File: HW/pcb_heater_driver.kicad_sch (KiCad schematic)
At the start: 9 parts

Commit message: Progress
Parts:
- removed PS?: (no value), symbol Converter_ACDC:IRM-60-12
- removed U?: (no value), Package_TO_SOT_SMD:SOT-23-5, symbol Regulator_Linear:AP2112K-3.3
- added H1, H2, H5, H7, H8: (no value), symbol Mechanical:MountingHole_Pad
- added H3: (no value), symbol Mechanical:MountingHole
- added H4: MH2, MountingHole:MountingHole_3.2mm_M3_Pad_TopBottom, symbol Mechanical:MountingHole_Pad
- added SW1: MAIN_SWITCH, symbol Switch:SW_SPST
- added U1: (no value), symbol Espressif:ESP32-S2-MINI-1
- C1: renamed from C?; value (none) -> C
- Q1: renamed from Q?; value BUK9M156-100EX -> (none)
- R1: renamed from R?; value (none) -> R
- R3: renamed from R?; value (none) -> 10k
- R4: renamed from R?; value (none) -> Heater - 1.5 Ohm
- gave numbers to parts that had none: 2
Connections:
- net +12V: now also SW1.1 (A)
- net GND: now also U1.1 (GND)
- net LIVE: now also H1.1
- net NEUTRAL: now also H2.1
- new net: U1.2 (GND), U1.30 (GND), U1.42 (GND), U1.43 (GND), U1.46 (GND), U1.47 (GND), U1.48 (GND), U1.49 (GND), U1.50 (GND), U1.51 (GND), U1.52 (GND), U1.53 (GND), U1.54 (GND), U1.55 (GND), U1.56 (GND), U1.57 (GND), U1.58 (GND), U1.59 (GND), U1.60 (GND), U1.61 (GND), U1.62 (GND), U1.63 (GND), U1.64 (GND), U1.65 (GND)
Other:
- note added: "AC/DC brick"
- note added: "Current monitor"
- note added: "Heater"
- note added: "I2C address is 0x.."
- note added: "Note: 5 A max current (60 W)"
- note added: "Note: RC filter description"
- moved on the sheet: C1, Q1, R1, R2, R3, R4, U2

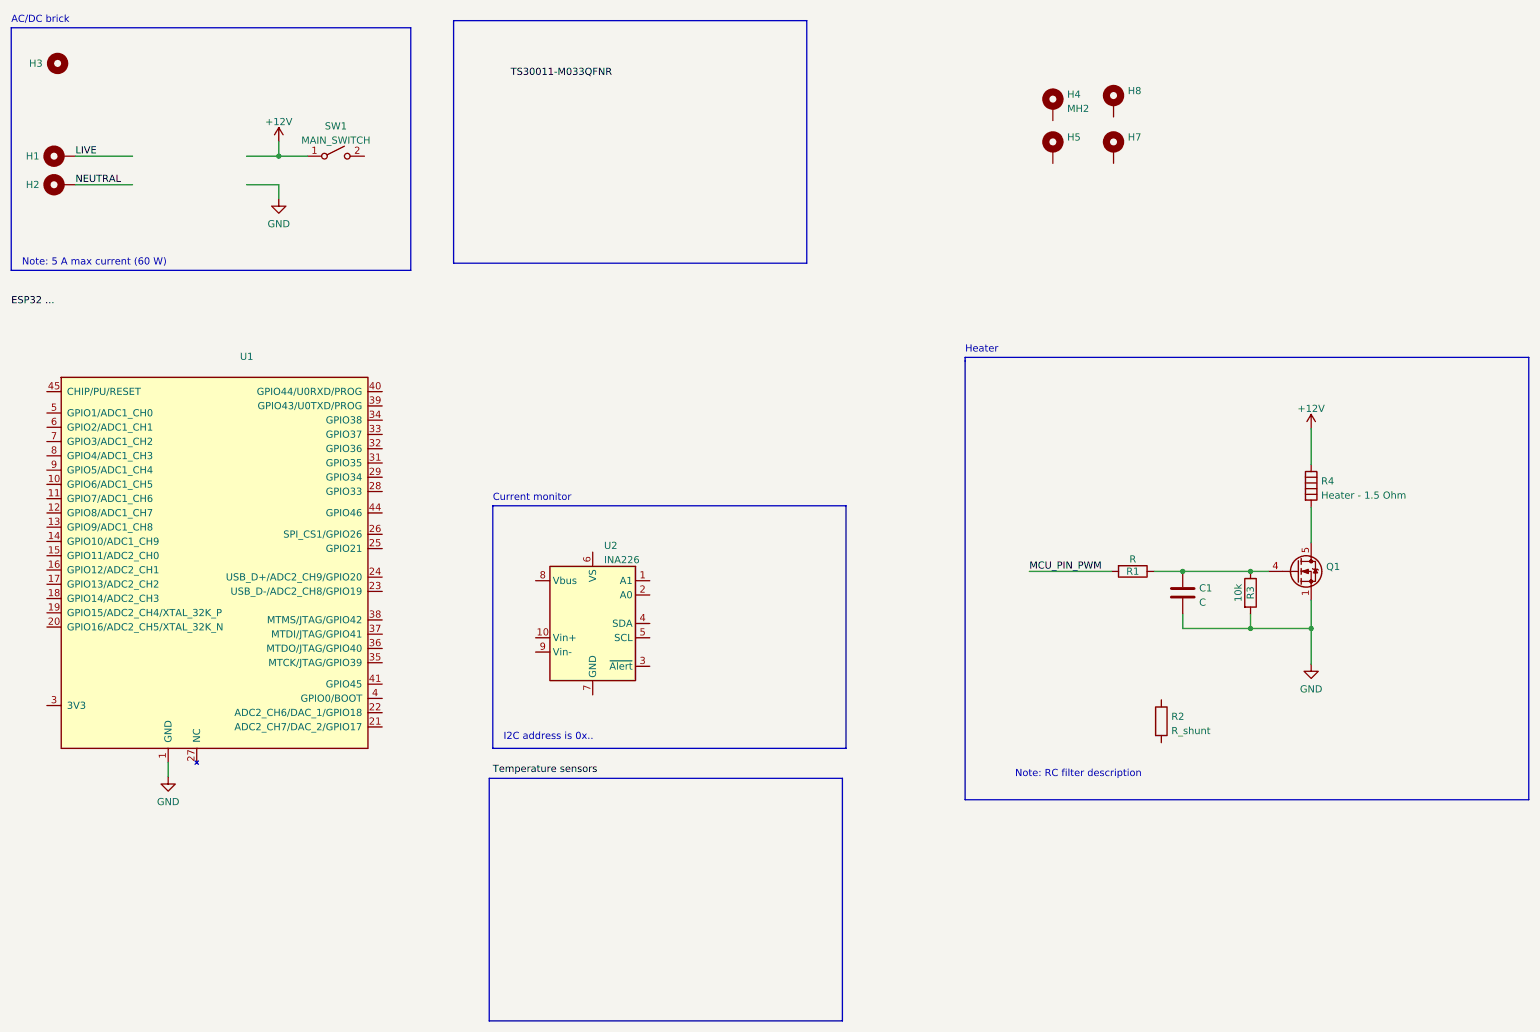
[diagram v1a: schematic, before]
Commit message: Sectioned schematic, reqorked heater trace length and thickness
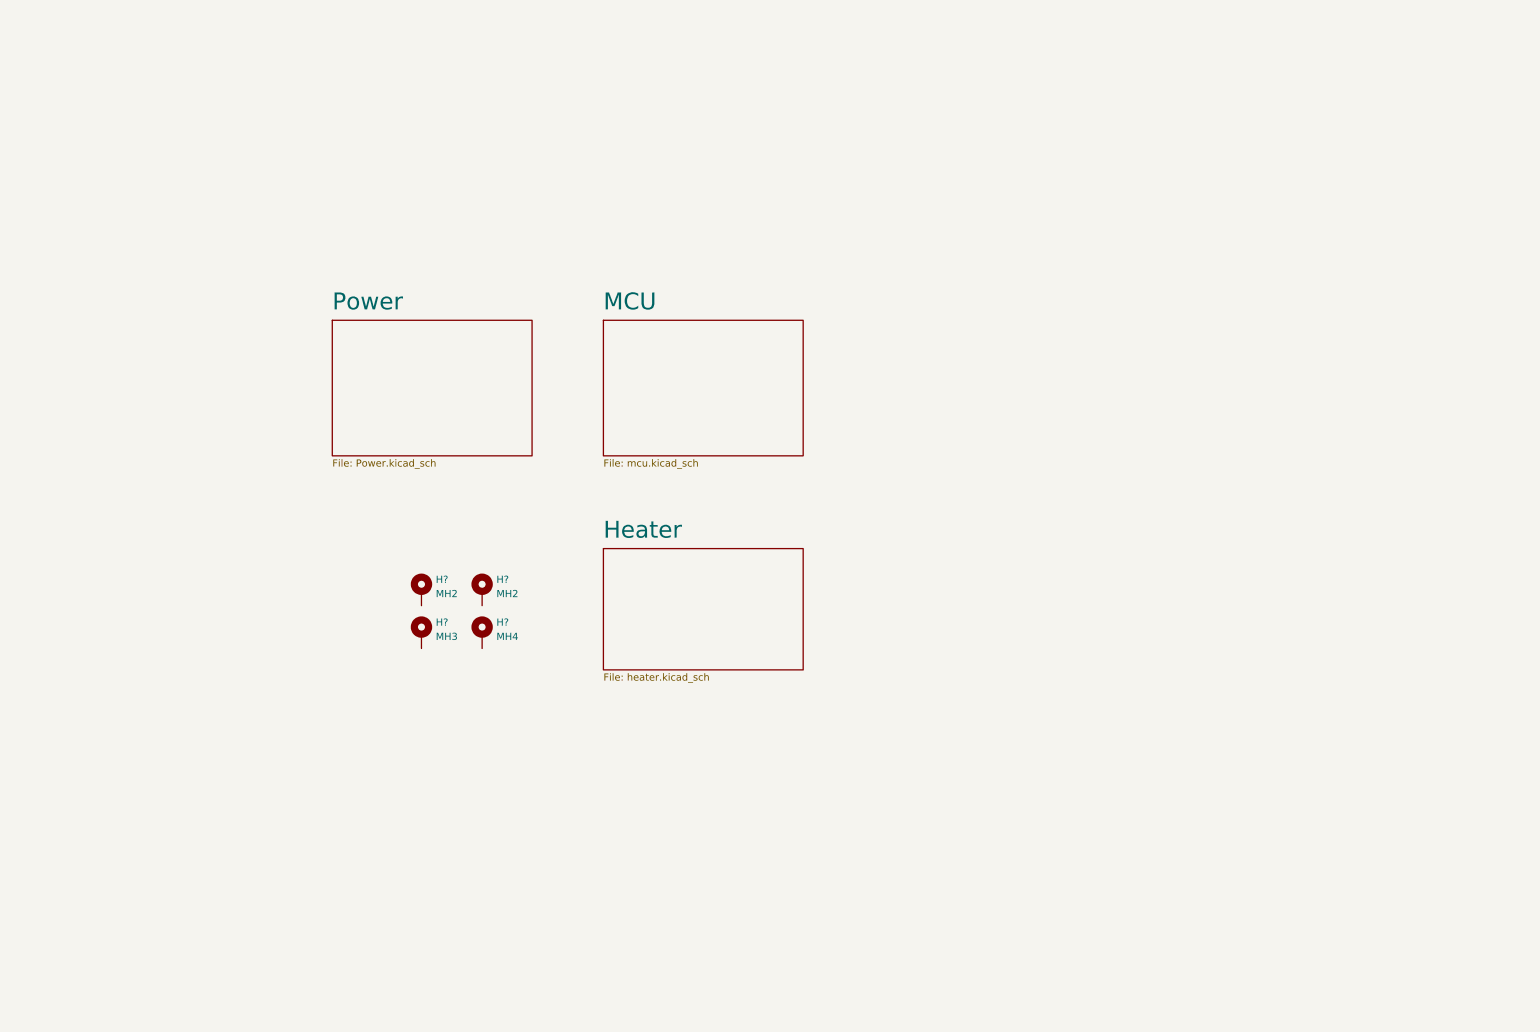
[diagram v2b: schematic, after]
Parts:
- removed C1: C, symbol Device:C
- removed H1, H2, H5, H7, H8: (no value), symbol Mechanical:MountingHole_Pad
- removed H3: (no value), symbol Mechanical:MountingHole
- removed H4: MH2, MountingHole:MountingHole_3.2mm_M3_Pad_TopBottom, symbol Mechanical:MountingHole_Pad
- removed Q1: (no value), Package_TO_SOT_SMD:LFPAK33, symbol Transistor_FET:BUK9M156-100EX
- removed R1: R, symbol Device:R
- removed R2: R_shunt, symbol Device:R
- removed R3: 10k, symbol Device:R
- removed R4: Heater - 1.5 Ohm, symbol Device:Heater
- removed SW1: MAIN_SWITCH, symbol Switch:SW_SPST
- removed U1: (no value), symbol Espressif:ESP32-S2-MINI-1
- removed U2: INA226, Package_SO:VSSOP-10_3x3mm_P0.5mm, symbol Analog_ADC:INA226
- added H?: MH3, MountingHole:MountingHole_3.2mm_M3_Pad_TopBottom, symbol Mechanical:MountingHole_Pad
- added H?: MH4, MountingHole:MountingHole_3.2mm_M3_Pad_TopBottom, symbol Mechanical:MountingHole_Pad
- added H? (x2): MH2, MountingHole:MountingHole_3.2mm_M3_Pad_TopBottom, symbol Mechanical:MountingHole_Pad
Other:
- added sheet Heater (heater.kicad_sch)
- added sheet MCU (mcu.kicad_sch)
- added sheet Power (Power.kicad_sch)
- note removed: "AC/DC brick"
- note removed: "Current monitor"
- note removed: "Heater"
- note removed: "I2C address is 0x.."
- note removed: "Note: 5 A max current (60 W)"
- note removed: "Note: RC filter description"

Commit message: Fixed board, big work in schematic, to finish
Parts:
- removed H?: MH3, MountingHole:MountingHole_3.2mm_M3_Pad_TopBottom, symbol Mechanical:MountingHole_Pad
- removed H?: MH4, MountingHole:MountingHole_3.2mm_M3_Pad_TopBottom, symbol Mechanical:MountingHole_Pad
- removed H? (x2): MH2, MountingHole:MountingHole_3.2mm_M3_Pad_TopBottom, symbol Mechanical:MountingHole_Pad
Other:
- sheet Heater: file heater.kicad_sch -> peripherals.kicad_sch

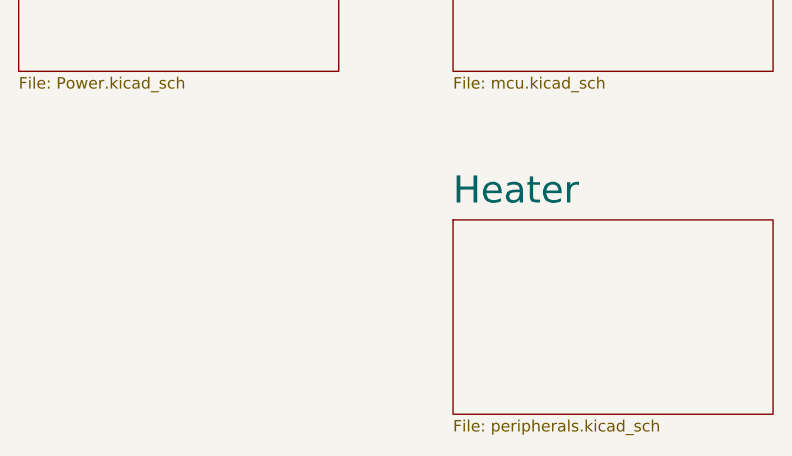
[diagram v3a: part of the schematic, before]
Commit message: Finished sch, to be checked. Initial components layout
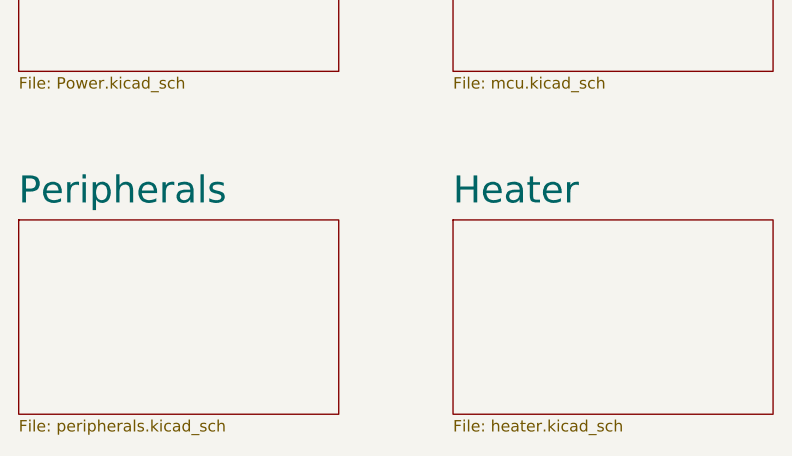
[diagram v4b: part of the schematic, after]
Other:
- added sheet Peripherals (peripherals.kicad_sch)
- sheet Heater: file peripherals.kicad_sch -> heater.kicad_sch
